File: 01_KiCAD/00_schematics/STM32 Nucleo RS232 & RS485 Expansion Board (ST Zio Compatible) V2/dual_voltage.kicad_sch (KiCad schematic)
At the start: 24 parts, among them U1 TLV77518PDBVR, U2 TPS2117DRLR

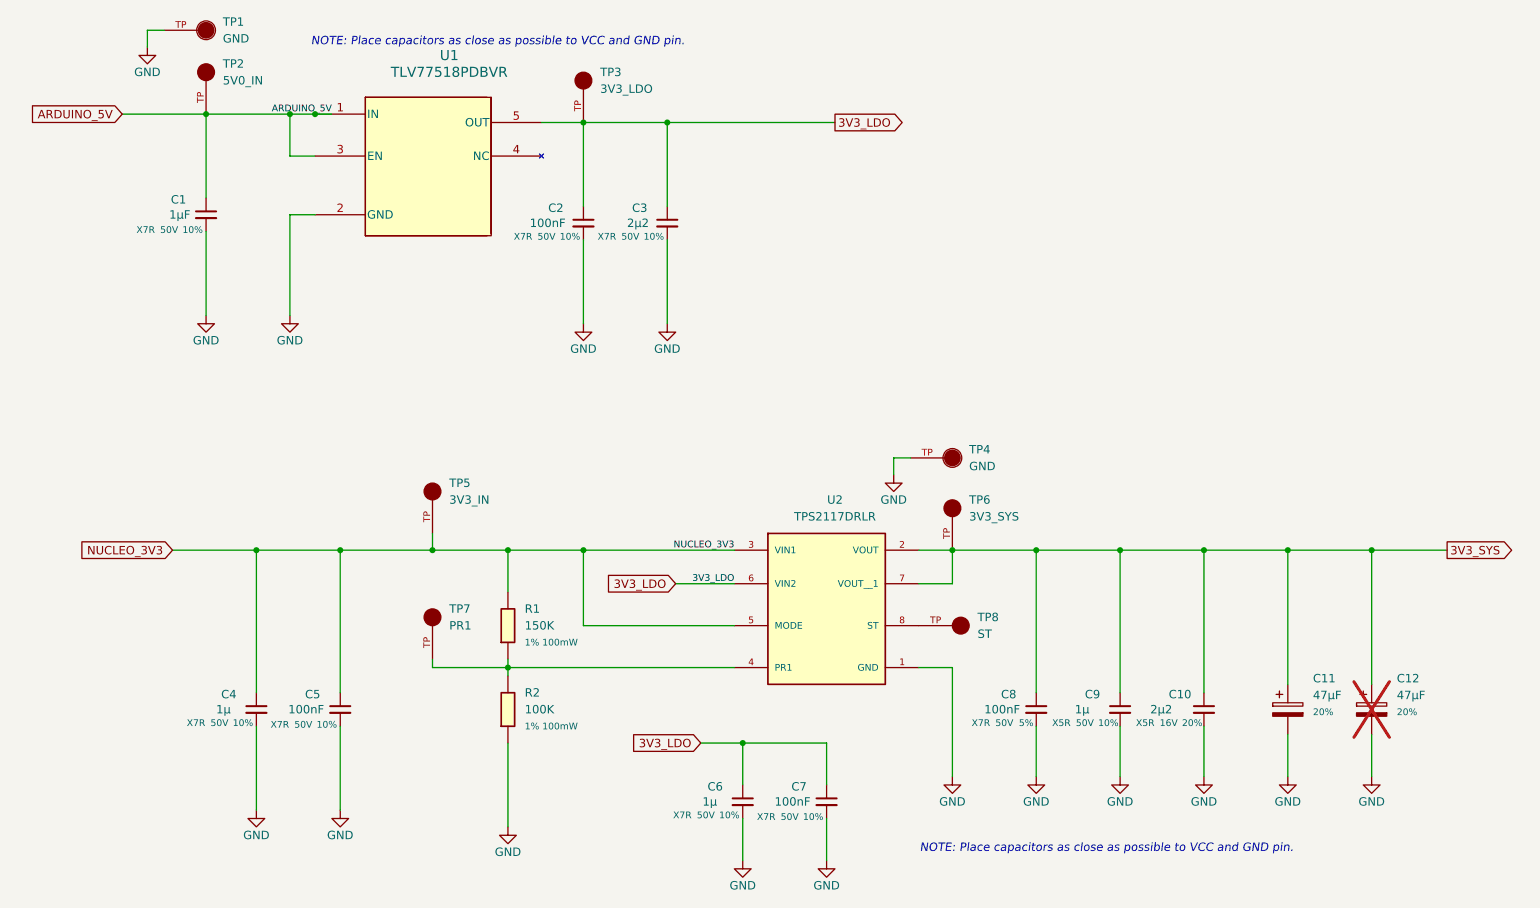
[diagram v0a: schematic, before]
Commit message: Updating routing
Update routing tracks and placing and re-ordering components on the board.
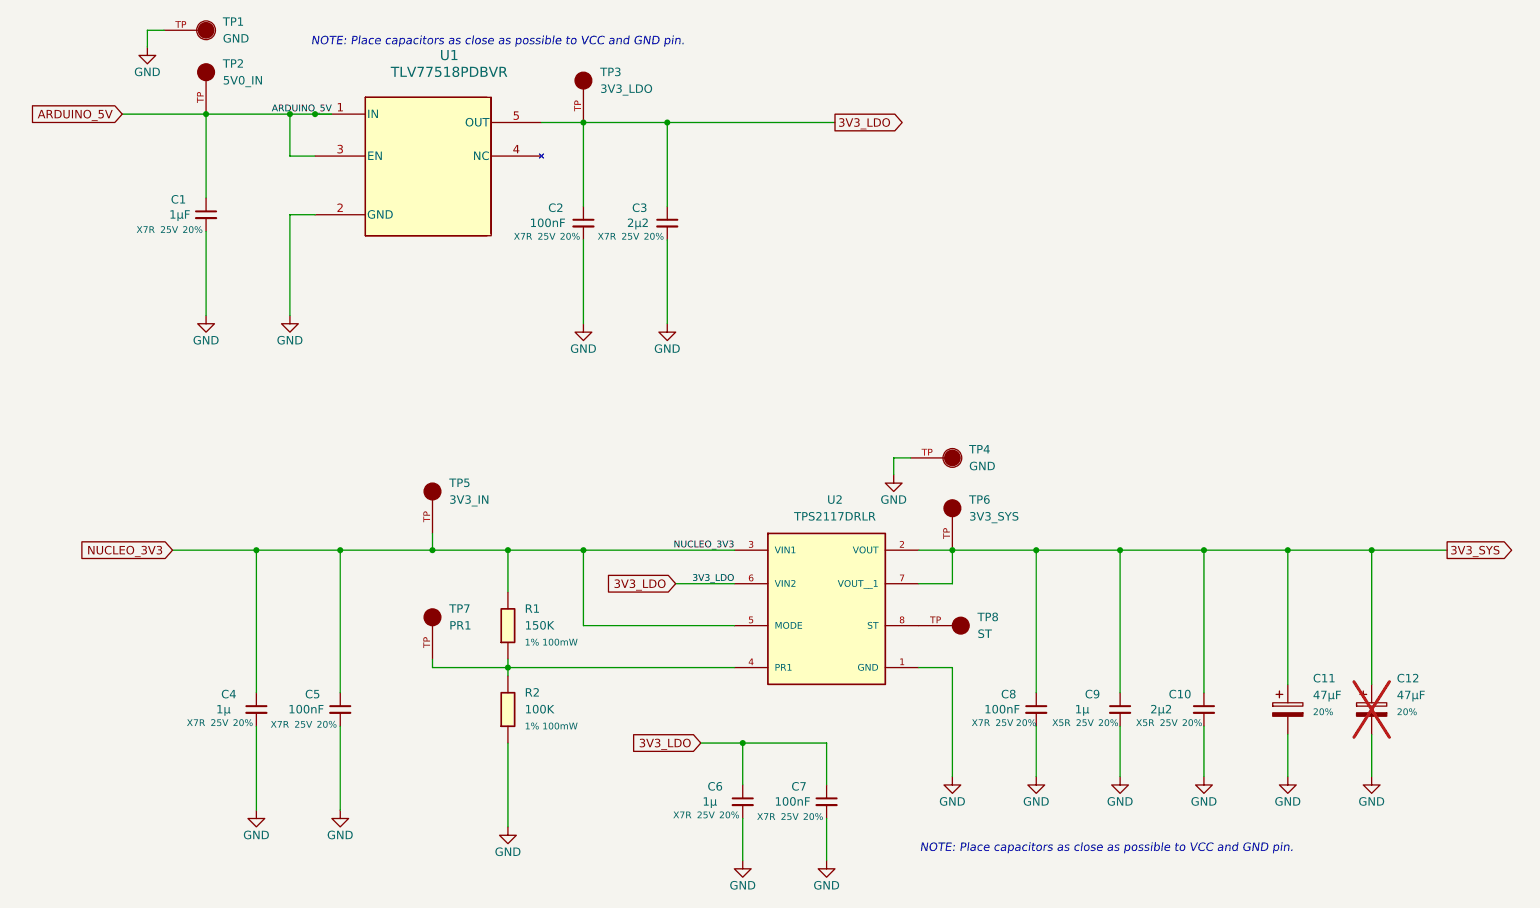
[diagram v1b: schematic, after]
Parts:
- C1, C9: footprint Capacitor_SMD:C_0805_2012Metric -> Capacitor_SMD:C_1206_3216Metric; PROD_ID (none) -> CAP-00810; Tolerance 10% -> 20%; Voltage 50V -> 25V
- C10: footprint Capacitor_SMD:C_1210_3225Metric -> Capacitor_SMD:C_1206_3216Metric; PROD_ID (none) -> CAP-00810; Voltage 16V -> 25V
- C2: Tolerance 10% -> 20%; Voltage 50V -> 25V
- C3, C4, C6: footprint Capacitor_SMD:C_0805_2012Metric -> Capacitor_SMD:C_1206_3216Metric; Tolerance 10% -> 20%; Voltage 50V -> 25V
- C5, C7: PROD_ID (none) -> CAP-00810; Tolerance 10% -> 20%; Voltage 50V -> 25V
- C8: footprint Capacitor_SMD:C_0603_1608Metric -> Capacitor_SMD:C_0805_2012Metric; PROD_ID (none) -> CAP-00810; Tolerance 5% -> 20%; Voltage 50V -> 25V
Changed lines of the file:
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@@
 			)
 		)
-		(property "Datasheet" "https://www.lcsc.com/datasheet/C577426.pdf"
+		(property "Datasheet" "https://cdn.sparkfun.com/assets/8/a/4/a/5/Kemet_Capacitor_Datasheet.pdf"
 			(at 90.17 142.24 0)
 			(effects
@@
 			)
 		)
-		(property "Description" "1uF X7R ±10% 50V 0805 Ceramic Capacitors RoHS"
+		(property "Description" "Unpolarized capacitor"
 			(at 90.17 147.32 0)
 			(effects
@@
 			)
 		)
-		(property "PROD_ID" ""
+		(property "PROD_ID" "CAP-00810"
 			(at 90.17 144.78 0)
 			(effects
@@
 			)
 		)
-		(property "Voltage" "50V"
+		(property "Voltage" "25V"
 			(at 84.582 130.556 0)
 			(effects
@@
 			)
 		)
-		(property "Tolerance" "10%"
+		(property "Tolerance" "20%"
 			(at 88.138 130.556 0)
 			(effects
@@
 			)
 		)
-		(property "Footprint" "Capacitor_SMD:C_0805_2012Metric"
+		(property "Footprint" "Capacitor_SMD:C_1206_3216Metric"
 			(at 208.28 139.7 0)
 			(effects
@@
 			)
 		)
-		(property "Datasheet" "https://www.lcsc.com/datasheet/C2932476.pdf"
+		(property "Datasheet" "https://cdn.sparkfun.com/assets/8/a/4/a/5/Kemet_Capacitor_Datasheet.pdf"
 			(at 208.28 142.24 0)
 			(effects
@@
 			)
 		)
-		(property "Description" "10uF ±10% 50V Ceramic Capacitor X5R 0805"
+		(property "Description" "Unpolarized capacitor"
 			(at 208.28 147.32 0)
 			(effects
@@
 			)
 		)
-		(property "PROD_ID" ""
+		(property "PROD_ID" "CAP-00810"
 			(at 208.28 144.78 0)
 			(effects
@@
 			)
 		)
-		(property "Voltage" "50V"
+		(property "Voltage" "25V"
 			(at 202.946 130.302 0)
 			(effects
@@
 			)
 		)
-		(property "Tolerance" "10%"
+		(property "Tolerance" "20%"
 			(at 206.502 130.302 0)
 			(effects
@@
 			)
 		)
-		(property "Footprint" "Capacitor_SMD:C_0805_2012Metric"
+		(property "Footprint" "Capacitor_SMD:C_1206_3216Metric"
 			(at 139.7 66.04 0)
 			(effects
@@
 			)
 		)
-		(property "Datasheet" "https://www.lcsc.com/datasheet/C125847.pdf"
+		(property "Datasheet" "https://cdn.sparkfun.com/assets/8/a/4/a/5/Kemet_Capacitor_Datasheet.pdf"
 			(at 139.7 68.58 0)
 			(effects
@@
 			)
 		)
-		(property "Description" "2.2uF ±10% 50V Ceramic Capacitor X7R 0805"
+		(property "Description" "Unpolarized capacitor"
 			(at 139.7 73.66 0)
 			(effects
@@
 			)
 		)
-		(property "Voltage" "50V"
+		(property "Voltage" "25V"
 			(at 134.112 56.642 0)
 			(effects
@@
 			)
 		)
-		(property "Tolerance" "10%"
+		(property "Tolerance" "20%"
 			(at 137.668 56.642 0)
 			(effects
@@
 			)
 		)
-		(property "Footprint" "Capacitor_SMD:C_1210_3225Metric"
+		(property "Footprint" "Capacitor_SMD:C_1206_3216Metric"
 			(at 220.98 139.7 0)
 			(effects
@@
 			)
 		)
-		(property "Datasheet" "https://www.lcsc.com/datasheet/C394395.pdf"
+		(property "Datasheet" "https://cdn.sparkfun.com/assets/8/a/4/a/5/Kemet_Capacitor_Datasheet.pdf"
 			(at 220.98 142.24 0)
 			(effects
@@
 			)
 		)
-		(property "Description" "100uF ±20% 16V Ceramic Capacitor X5R 1210"
+		(property "Description" "Unpolarized capacitor"
 			(at 220.98 147.32 0)
 			(effects
@@
 			)
 		)
-		(property "PROD_ID" ""
+		(property "PROD_ID" "CAP-00810"
 			(at 220.98 144.78 0)
 			(effects
@@
 			)
 		)
-		(property "Voltage" "16V"
+		(property "Voltage" "25V"
 			(at 215.646 130.302 0)
 			(effects
@@
 			)
 		)
-		(property "Datasheet" "https://www.lcsc.com/datasheet/C577426.pdf"
+		(property "Datasheet" "https://cdn.sparkfun.com/assets/8/a/4/a/5/Kemet_Capacitor_Datasheet.pdf"
 			(at 163.83 156.21 0)
 			(effects
@@
 			)
 		)
-		(property "Description" "1uF X7R ±10% 50V 0805 Ceramic Capacitors RoHS"
+		(property "Description" "Unpolarized capacitor"
 			(at 163.83 161.29 0)
 			(effects
@@
 			)
 		)
-		(property "PROD_ID" ""
+		(property "PROD_ID" "CAP-00810"
 			(at 163.83 158.75 0)
 			(effects
@@
 			)
 		)
-		(property "Voltage" "50V"
+		(property "Voltage" "25V"
 			(at 158.242 144.526 0)
 			(effects
@@
 			)
 		)
-		(property "Tolerance" "10%"
+		(property "Tolerance" "20%"
 			(at 161.798 144.526 0)
 			(effects
@@
 			)
 		)
-		(property "Footprint" "Capacitor_SMD:C_0805_2012Metric"
+		(property "Footprint" "Capacitor_SMD:C_1206_3216Metric"
 			(at 77.47 139.7 0)
 			(effects
@@
 			)
 		)
-		(property "Datasheet" "https://www.lcsc.com/datasheet/C125847.pdf"
+		(property "Datasheet" "https://cdn.sparkfun.com/assets/8/a/4/a/5/Kemet_Capacitor_Datasheet.pdf"
 			(at 77.47 142.24 0)
 			(effects
@@
 			)
 		)
-		(property "Description" "2.2uF ±10% 50V Ceramic Capacitor X7R 0805"
+		(property "Description" "Unpolarized capacitor"
 			(at 77.47 147.32 0)
 			(effects
@@
 			)
 		)
-		(property "Voltage" "50V"
+		(property "Voltage" "25V"
 			(at 71.882 130.302 0)
 			(effects
@@
 			)
 		)
-		(property "Tolerance" "10%"
+		(property "Tolerance" "20%"
 			(at 75.438 130.302 0)
 			(effects
@@
 			)
 		)
-		(property "Footprint" "Capacitor_SMD:C_0805_2012Metric"
+		(property "Footprint" "Capacitor_SMD:C_1206_3216Metric"
 			(at 151.13 153.67 0)
 			(effects
@@
 			)
 		)
-		(property "Datasheet" "https://www.lcsc.com/datasheet/C125847.pdf"
+		(property "Datasheet" "https://cdn.sparkfun.com/assets/8/a/4/a/5/Kemet_Capacitor_Datasheet.pdf"
 			(at 151.13 156.21 0)
 			(effects
@@
 			)
 		)
-		(property "Description" "2.2uF ±10% 50V Ceramic Capacitor X7R 0805"
+		(property "Description" "Unpolarized capacitor"
 			(at 151.13 161.29 0)
 			(effects
@@
 			)
 		)
-		(property "Voltage" "50V"
+		(property "Voltage" "25V"
 			(at 145.542 144.272 0)
 			(effects
@@
 			)
 		)
-		(property "Tolerance" "10%"
+		(property "Tolerance" "20%"
 			(at 149.098 144.272 0)
 			(effects
@@
 			)
 		)
-		(property "Datasheet" "https://www.lcsc.com/datasheet/C125847.pdf"
+		(property "Datasheet" "https://cdn.sparkfun.com/assets/8/a/4/a/5/Kemet_Capacitor_Datasheet.pdf"
 			(at 127 68.58 0)
 			(effects
@@
 			)
 		)
-		(property "Description" "2.2uF ±10% 50V Ceramic Capacitor X7R 0805"
+		(property "Description" "Unpolarized capacitor"
 			(at 127 73.66 0)
 			(effects
@@
 			)
 		)
-		(property "Voltage" "50V"
+		(property "Voltage" "25V"
 			(at 121.412 56.642 0)
 			(effects
@@
 			)
 		)
-		(property "Tolerance" "10%"
+		(property "Tolerance" "20%"
 			(at 124.968 56.642 0)
 			(effects
@@
 			)
 		)
-		(property "Footprint" "Capacitor_SMD:C_0603_1608Metric"
+		(property "Footprint" "Capacitor_SMD:C_0805_2012Metric"
 			(at 195.58 139.7 0)
 			(effects
@@
 			)
 		)
-		(property "Datasheet" "https://www.lcsc.com/datasheet/C24452.pdf"
+		(property "Datasheet" "https://cdn.sparkfun.com/assets/8/a/4/a/5/Kemet_Capacitor_Datasheet.pdf"
 			(at 195.58 142.24 0)
 			(effects
@@
 			)
 		)
-		(property "Description" "100nF ±5% 50V Ceramic Capacitor X7R 0603"
+		(property "Description" "Unpolarized capacitor"
 			(at 195.58 147.32 0)
 			(effects
@@
 			)
 		)
-		(property "PROD_ID" ""
+		(property "PROD_ID" "CAP-00810"
 			(at 195.58 144.78 0)
 			(effects
@@
 			)
 		)
-		(property "Voltage" "50V"
+		(property "Voltage" "25V"
 			(at 190.754 130.302 0)
 			(effects
@@
 			)
 		)
-		(property "Tolerance" "5%"
+		(property "Tolerance" "20%"
 			(at 194.056 130.302 0)
 			(effects
@@
 			)
 		)
-		(property "Footprint" "Capacitor_SMD:C_0805_2012Metric"
+		(property "Footprint" "Capacitor_SMD:C_1206_3216Metric"
 			(at 69.85 64.77 0)
 			(effects
@@
 			)
 		)
-		(property "Datasheet" "https://www.lcsc.com/datasheet/C577426.pdf"
+		(property "Datasheet" "https://cdn.sparkfun.com/assets/8/a/4/a/5/Kemet_Capacitor_Datasheet.pdf"
 			(at 69.85 67.31 0)
 			(effects
@@
 			)
 		)
-		(property "Description" "1uF X7R ±10% 50V 0805 Ceramic Capacitors RoHS"
+		(property "Description" "Unpolarized capacitor"
 			(at 69.85 72.39 0)
 			(effects
@@
 			)
 		)
-		(property "PROD_ID" ""
+		(property "PROD_ID" "CAP-00810"
 			(at 69.85 69.85 0)
 			(effects
@@
 			)
 		)
-		(property "Voltage" "50V"
+		(property "Voltage" "25V"
 			(at 64.262 55.626 0)
 			(effects
@@
 			)
 		)
-		(property "Tolerance" "10%"
+		(property "Tolerance" "20%"
 			(at 67.818 55.626 0)
 			(effects
